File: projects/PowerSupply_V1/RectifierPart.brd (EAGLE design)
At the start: 50 x 50 mm, 17 parts, among them X1 IN, X2 PRI, X3 SEC, X4 OUT

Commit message: feat: rectifier power sources modified
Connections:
- new net +15VAC: F2.1, X3.1
- new net +20V: C1.1, C3.1, C5.+, D1.C, D3.C, X4.1
- new net -15VAC: C3.2, C4.1, D3.A, D4.C, X3.4
- new net -20V: C2.2, C4.2, C6.-, D2.A, D4.A, X4.3
- net V+: no longer C1.1, C3.1, C5.+, D1.C, D3.C, F2.1, X3.1, X4.1
- net V-: no longer C2.2, C3.2, C4.1, C4.2, C6.-, D2.A, D3.A, D4.A, D4.C, X3.4, X4.3
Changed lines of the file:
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@@
 <contactref element="F1" pad="2"/>
 <contactref element="R1" pad="2"/>
-<contactref element="X3" pad="1"/>
-<contactref element="F2" pad="1"/>
-<contactref element="D1" pad="C"/>
-<contactref element="D3" pad="C"/>
-<contactref element="C1" pad="1"/>
-<contactref element="C3" pad="1"/>
-<contactref element="C5" pad="+"/>
-<contactref element="X4" pad="1"/>
-<wire x1="45.847" y1="8.636" x2="45.847" y2="24.13" width="0" layer="19" extent="1-1"/>
-<wire x1="32.258" y1="4.572" x2="45.847" y2="8.636" width="0" layer="19" extent="1-1"/>
-<wire x1="4.191" y1="39.37" x2="45.847" y2="24.13" width="0" layer="19" extent="1-1"/>
 <wire x1="-14.1478" y1="31.75" x2="4.191" y2="39.37" width="0" layer="19" extent="1-1"/>
 <wire x1="-14.859" y1="16.51" x2="-14.1478" y2="31.75" width="0" layer="19" extent="1-1"/>
-<wire x1="-63.3222" y1="31.75" x2="-14.1478" y2="31.75" width="0" layer="19" extent="1-1"/>
-<wire x1="-63.5" y1="53.34" x2="-63.3222" y2="31.75" width="0" layer="19" extent="1-1"/>
-<wire x1="-50.8" y1="66.04" x2="-63.5" y2="53.34" width="0" layer="19" extent="1-1"/>
-<wire x1="-54.61" y1="74.93" x2="-50.8" y2="66.04" width="0" layer="19" extent="1-1"/>
-<wire x1="-39.37" y1="74.93" x2="-50.8" y2="66.04" width="0" layer="19" extent="1-1"/>
 </signal>
 <signal name="V-">
@@
 <contactref element="X2" pad="4"/>
 <contactref element="R1" pad="1"/>
-<contactref element="X3" pad="4"/>
-<contactref element="D3" pad="A"/>
-<contactref element="D4" pad="C"/>
-<contactref element="C3" pad="2"/>
-<contactref element="C4" pad="1"/>
-<contactref element="D2" pad="A"/>
-<contactref element="D4" pad="A"/>
-<contactref element="C2" pad="2"/>
-<contactref element="C4" pad="2"/>
-<contactref element="C6" pad="-"/>
-<contactref element="X4" pad="3"/>
-<wire x1="32.258" y1="28.956" x2="45.847" y2="39.37" width="0" layer="19" extent="1-1"/>
-<wire x1="45.847" y1="18.796" x2="32.258" y2="28.956" width="0" layer="19" extent="1-1"/>
-<wire x1="4.191" y1="34.29" x2="32.258" y2="28.956" width="0" layer="19" extent="1-1"/>
 <wire x1="4.191" y1="8.636" x2="4.191" y2="34.29" width="0" layer="19" extent="1-1"/>
 <wire x1="-18.161" y1="6.35" x2="4.191" y2="8.636" width="0" layer="19" extent="1-1"/>
-<wire x1="-15.24" y1="66.04" x2="4.191" y2="34.29" width="0" layer="19" extent="1-1"/>
-<wire x1="-15.24" y1="74.93" x2="-15.24" y2="66.04" width="0" layer="19" extent="1-1"/>
-<wire x1="-30.48" y1="74.93" x2="-15.24" y2="74.93" width="0" layer="19" extent="1-1"/>
-<wire x1="-35.56" y1="66.04" x2="-30.48" y2="74.93" width="0" layer="19" extent="1-1"/>
-<wire x1="-41.91" y1="74.93" x2="-35.56" y2="66.04" width="0" layer="19" extent="1-1"/>
-<wire x1="-49.53" y1="74.93" x2="-41.91" y2="74.93" width="0" layer="19" extent="1-1"/>
-<wire x1="-57.15" y1="74.93" x2="-49.53" y2="74.93" width="0" layer="19" extent="1-1"/>
-<wire x1="-62.23" y1="74.93" x2="-57.15" y2="74.93" width="0" layer="19" extent="1-1"/>
 </signal>
 <signal name="N$2">
@@
 <wire x1="-40.8178" y1="31.75" x2="-48.26" y2="53.34" width="0" layer="19" extent="1-1"/>
 </signal>
+<signal name="+20V">
+<contactref element="X4" pad="1"/>
+<contactref element="D1" pad="C"/>
+<contactref element="D3" pad="C"/>
+<contactref element="C1" pad="1"/>
+<contactref element="C3" pad="1"/>
+<contactref element="C5" pad="+"/>
+<wire x1="32.258" y1="4.572" x2="45.847" y2="8.636" width="0" layer="19" extent="1-1"/>
+<wire x1="-39.37" y1="74.93" x2="32.258" y2="4.572" width="0" layer="19" extent="1-1"/>
+<wire x1="-50.8" y1="66.04" x2="-39.37" y2="74.93" width="0" layer="19" extent="1-1"/>
+<wire x1="-54.61" y1="74.93" x2="-50.8" y2="66.04" width="0" layer="19" extent="1-1"/>
+<wire x1="-63.5" y1="53.34" x2="-50.8" y2="66.04" width="0" layer="19" extent="1-1"/>
+</signal>
+<signal name="-20V">
+<contactref element="X4" pad="3"/>
+<contactref element="D2" pad="A"/>
+<contactref element="D4" pad="A"/>
+<contactref element="C2" pad="2"/>
+<contactref element="C4" pad="2"/>
+<contactref element="C6" pad="-"/>
+<wire x1="32.258" y1="28.956" x2="45.847" y2="18.796" width="0" layer="19" extent="1-1"/>
+<wire x1="-15.24" y1="66.04" x2="32.258" y2="28.956" width="0" layer="19" extent="1-1"/>
+<wire x1="-15.24" y1="74.93" x2="-15.24" y2="66.04" width="0" layer="19" extent="1-1"/>
+<wire x1="-41.91" y1="74.93" x2="-15.24" y2="74.93" width="0" layer="19" extent="1-1"/>
+<wire x1="-57.15" y1="74.93" x2="-41.91" y2="74.93" width="0" layer="19" extent="1-1"/>
+</signal>
+<signal name="+15VAC">
+<contactref element="X3" pad="1"/>
+<contactref element="F2" pad="1"/>
+<wire x1="-63.3222" y1="31.75" x2="45.847" y2="24.13" width="0" layer="19" extent="1-1"/>
+</signal>
+<signal name="-15VAC">
+<contactref element="X3" pad="4"/>
+<contactref element="D3" pad="A"/>
+<contactref element="D4" pad="C"/>
+<contactref element="C3" pad="2"/>
+<contactref element="C4" pad="1"/>
+<wire x1="-30.48" y1="74.93" x2="45.847" y2="39.37" width="0" layer="19" extent="1-1"/>
+<wire x1="-35.56" y1="66.04" x2="-30.48" y2="74.93" width="0" layer="19" extent="1-1"/>
+<wire x1="-49.53" y1="74.93" x2="-35.56" y2="66.04" width="0" layer="19" extent="1-1"/>
+<wire x1="-62.23" y1="74.93" x2="-49.53" y2="74.93" width="0" layer="19" extent="1-1"/>
+</signal>
 </signals>

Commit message: feat: rectifier part modified
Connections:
- net V+ renamed +230VAC
- removed net V-: R1.1, X1.2, X2.4
- new net -230VAC: R1.1, X1.3, X2.4
- net PE: now also X1.2; no longer X1.3
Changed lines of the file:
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@@
 <signals>
 <signal name="GND">
-<contactref element="X3" pad="2"/>
-<contactref element="X3" pad="3"/>
 <contactref element="C6" pad="+"/>
 <contactref element="C5" pad="-"/>
 <contactref element="X4" pad="2"/>
+<contactref element="X3" pad="3"/>
+<contactref element="X3" pad="2"/>
 <wire x1="45.847" y1="29.21" x2="45.847" y2="34.29" width="0" layer="19" extent="1-1"/>
 <wire x1="45.847" y1="13.716" x2="45.847" y2="29.21" width="0" layer="19" extent="1-1"/>
 <wire x1="32.258" y1="12.192" x2="45.847" y2="13.716" width="0" layer="19" extent="1-1"/>
 <wire x1="32.258" y1="21.336" x2="32.258" y2="12.192" width="0" layer="19" extent="1-1"/>
-</signal>
-<signal name="PE">
-<contactref element="X1" pad="3"/>
-</signal>
-<signal name="V+">
-<contactref element="X1" pad="1"/>
-<contactref element="F1" pad="2"/>
-<contactref element="R1" pad="2"/>
-<wire x1="-14.1478" y1="31.75" x2="4.191" y2="39.37" width="0" layer="19" extent="1-1"/>
-<wire x1="-14.859" y1="16.51" x2="-14.1478" y2="31.75" width="0" layer="19" extent="1-1"/>
-</signal>
-<signal name="V-">
-<contactref element="X1" pad="2"/>
-<contactref element="X2" pad="4"/>
-<contactref element="R1" pad="1"/>
-<wire x1="4.191" y1="8.636" x2="4.191" y2="34.29" width="0" layer="19" extent="1-1"/>
-<wire x1="-18.161" y1="6.35" x2="4.191" y2="8.636" width="0" layer="19" extent="1-1"/>
 </signal>
 <signal name="N$2">
@@
 <wire x1="-40.8178" y1="31.75" x2="-48.26" y2="53.34" width="0" layer="19" extent="1-1"/>
 </signal>
-<signal name="+20V">
-<contactref element="X4" pad="1"/>
-<contactref element="D1" pad="C"/>
-<contactref element="D3" pad="C"/>
-<contactref element="C1" pad="1"/>
-<contactref element="C3" pad="1"/>
-<contactref element="C5" pad="+"/>
-<wire x1="32.258" y1="4.572" x2="45.847" y2="8.636" width="0" layer="19" extent="1-1"/>
-<wire x1="-39.37" y1="74.93" x2="32.258" y2="4.572" width="0" layer="19" extent="1-1"/>
-<wire x1="-50.8" y1="66.04" x2="-39.37" y2="74.93" width="0" layer="19" extent="1-1"/>
-<wire x1="-54.61" y1="74.93" x2="-50.8" y2="66.04" width="0" layer="19" extent="1-1"/>
-<wire x1="-63.5" y1="53.34" x2="-50.8" y2="66.04" width="0" layer="19" extent="1-1"/>
+<signal name="PE">
+<contactref element="X1" pad="2"/>
 </signal>
-<signal name="-20V">
-<contactref element="X4" pad="3"/>
-<contactref element="D2" pad="A"/>
-<contactref element="D4" pad="A"/>
-<contactref element="C2" pad="2"/>
-<contactref element="C4" pad="2"/>
-<contactref element="C6" pad="-"/>
-<wire x1="32.258" y1="28.956" x2="45.847" y2="18.796" width="0" layer="19" extent="1-1"/>
-<wire x1="-15.24" y1="66.04" x2="32.258" y2="28.956" width="0" layer="19" extent="1-1"/>
-<wire x1="-15.24" y1="74.93" x2="-15.24" y2="66.04" width="0" layer="19" extent="1-1"/>
-<wire x1="-41.91" y1="74.93" x2="-15.24" y2="74.93" width="0" layer="19" extent="1-1"/>
-<wire x1="-57.15" y1="74.93" x2="-41.91" y2="74.93" width="0" layer="19" extent="1-1"/>
+<signal name="+230VAC">
+<contactref element="X1" pad="1"/>
+<contactref element="F1" pad="2"/>
+<contactref element="R1" pad="2"/>
+<wire x1="-14.1478" y1="31.75" x2="4.191" y2="39.37" width="0" layer="19" extent="1-1"/>
+<wire x1="-14.859" y1="16.51" x2="-14.1478" y2="31.75" width="0" layer="19" extent="1-1"/>
+</signal>
+<signal name="-230VAC">
+<contactref element="X1" pad="3"/>
+<contactref element="X2" pad="4"/>
+<contactref element="R1" pad="1"/>
+<wire x1="4.191" y1="8.636" x2="4.191" y2="29.21" width="0" layer="19" extent="1-1"/>
+<wire x1="-18.161" y1="6.35" x2="4.191" y2="8.636" width="0" layer="19" extent="1-1"/>
 </signal>
 <signal name="+15VAC">
@@
 <wire x1="-62.23" y1="74.93" x2="-49.53" y2="74.93" width="0" layer="19" extent="1-1"/>
 </signal>
+<signal name="-20V">
+<contactref element="X4" pad="3"/>
+<contactref element="D2" pad="A"/>
+<contactref element="D4" pad="A"/>
+<contactref element="C2" pad="2"/>
+<contactref element="C4" pad="2"/>
+<contactref element="C6" pad="-"/>
+<wire x1="32.258" y1="28.956" x2="45.847" y2="18.796" width="0" layer="19" extent="1-1"/>
+<wire x1="-15.24" y1="66.04" x2="32.258" y2="28.956" width="0" layer="19" extent="1-1"/>
+<wire x1="-15.24" y1="74.93" x2="-15.24" y2="66.04" width="0" layer="19" extent="1-1"/>
+<wire x1="-41.91" y1="74.93" x2="-15.24" y2="74.93" width="0" layer="19" extent="1-1"/>
+<wire x1="-57.15" y1="74.93" x2="-41.91" y2="74.93" width="0" layer="19" extent="1-1"/>
+</signal>
+<signal name="+20V">
+<contactref element="X4" pad="1"/>
+<contactref element="D1" pad="C"/>
+<contactref element="D3" pad="C"/>
+<contactref element="C1" pad="1"/>
+<contactref element="C3" pad="1"/>
+<contactref element="C5" pad="+"/>
+<wire x1="32.258" y1="4.572" x2="45.847" y2="8.636" width="0" layer="19" extent="1-1"/>
+<wire x1="-39.37" y1="74.93" x2="32.258" y2="4.572" width="0" layer="19" extent="1-1"/>
+<wire x1="-50.8" y1="66.04" x2="-39.37" y2="74.93" width="0" layer="19" extent="1-1"/>
+<wire x1="-54.61" y1="74.93" x2="-50.8" y2="66.04" width="0" layer="19" extent="1-1"/>
+<wire x1="-63.5" y1="53.34" x2="-50.8" y2="66.04" width="0" layer="19" extent="1-1"/>
+</signal>
 </signals>

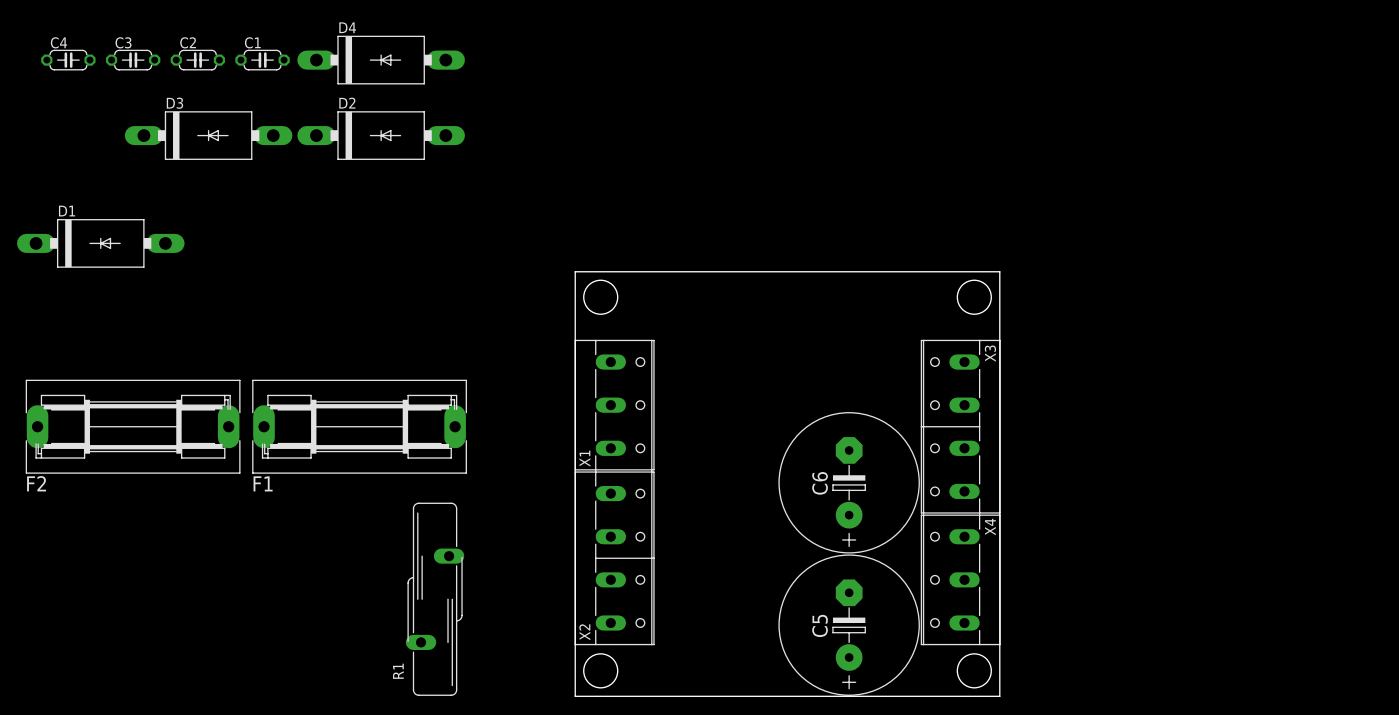
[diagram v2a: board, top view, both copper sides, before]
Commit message: feat: rectifier part refactored
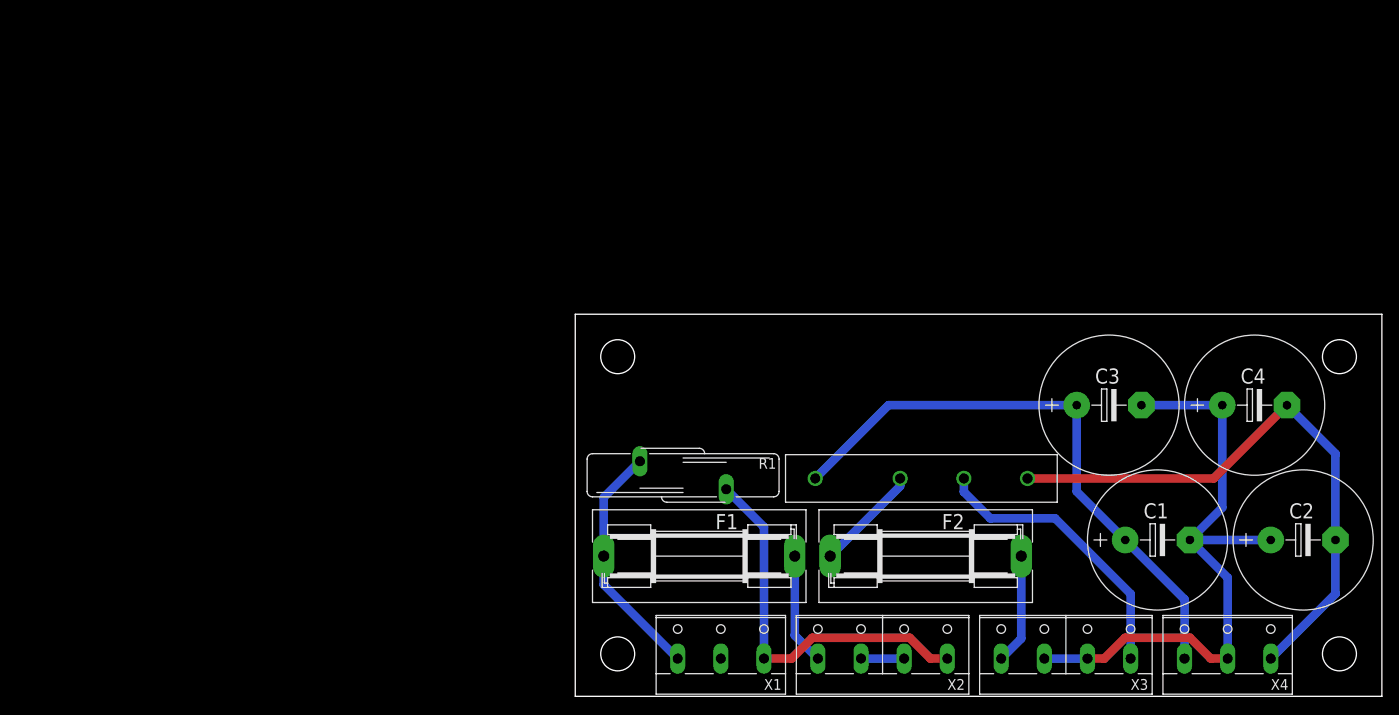
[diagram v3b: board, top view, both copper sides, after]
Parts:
- removed C5, C6: 2200µF, rcl:E7,5-16
- removed D1, D2, D3, D4: 10U45SD1, diode:DO201-15
- added R+1: B40C5000-3300A, bb84:B..C
- C1, C2, C3, C4: value 10nF -> 2200µF; device rcl:C050-024X044 -> rcl:E7,5-16
- moved C4 145.5 mm to (80.0, 34.3)
- moved C2 141.9 mm to (85.7, 18.4)
- moved C3 121.9 mm to (62.9, 34.3)
- moved C1 119.6 mm to (68.6, 18.4)
- moved F2 94.6 mm to (41.3, 16.5), turned to 180 degrees
- moved F1 42.8 mm to (14.6, 16.5), turned to 180 degrees
- moved X2 33.3 mm to (36.2, 5.08), turned to 0 degrees
- moved X4 32.8 mm to (76.8, 5.08), turned to 0 degrees
- moved R1 32.7 mm to (12.7, 26.0), turned to 90 degrees
- moved X1 31.7 mm to (17.1, 5.08), turned to 0 degrees
- moved X3 29.5 mm to (57.8, 5.08), turned to 0 degrees
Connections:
- removed net N$5: C1.2, C2.1, D1.A, D2.C, F2.2
- new net N$1: F2.2, R+1.~VAC1
- net +20V: now also C1.+, C3.+, R+1.+VDC; no longer C1.1, C3.1, C5.+, D1.C, D3.C
- net -15VAC: now also R+1.~VAC2; no longer C3.2, C4.1, D3.A, D4.C
- net -20V: now also C2.-, C4.-, R+1.-VDC; no longer C2.2, C4.2, C6.-, D2.A, D4.A
- net GND: now also C1.-, C2.+, C3.-, C4.+; no longer C5.-, C6.+
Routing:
- net GND: track 0.00 -> 75.9 mm
- net -20V: track 0.00 -> 69.5 mm
- net +20V: track 0.00 -> 69.5 mm
- net -230VAC: track 0.00 -> 45.4 mm
- net -15VAC: track 0.00 -> 33.8 mm
- net +230VAC: track 0.00 -> 28.6 mm
- net N$3: track 0.00 -> 13.2 mm
- net +15VAC: track 0.00 -> 13.0 mm
- net N$1: track 0.00 -> 12.6 mm
- net N$2: track 0.00 -> 5.08 mm
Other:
- board size 50 x 50 mm -> 95 x 45 mm

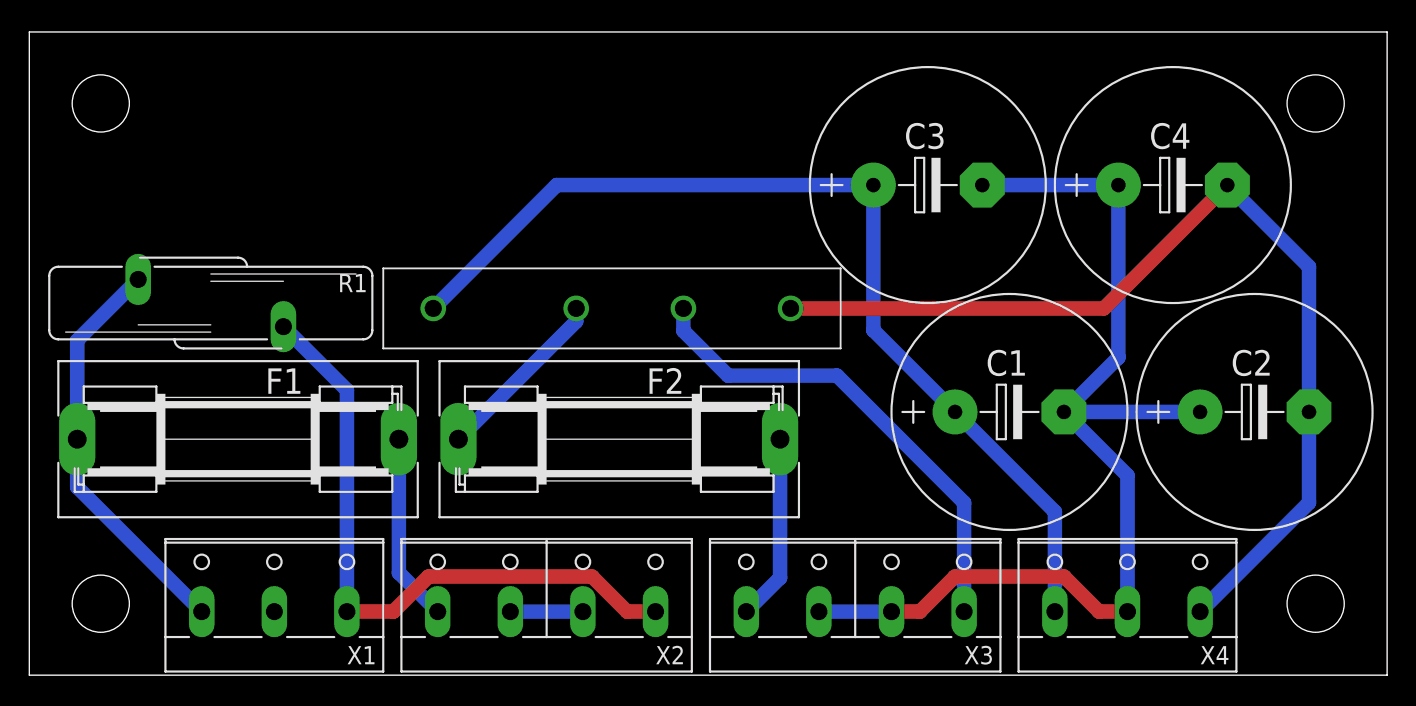
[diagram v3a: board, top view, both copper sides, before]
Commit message: feat: rectifier part modified
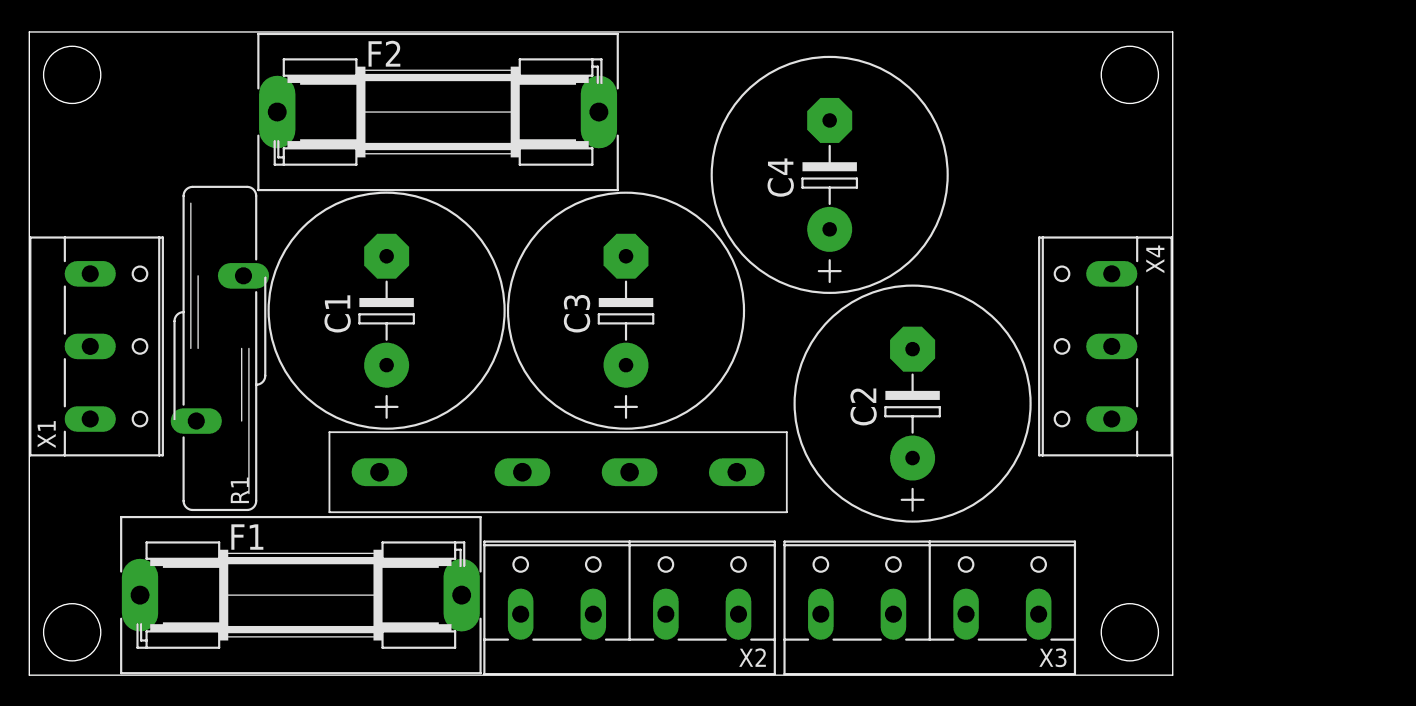
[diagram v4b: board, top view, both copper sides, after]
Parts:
- moved C1 44.2 mm to (25.0, 25.5), turned to 90 degrees
- moved F2 26.2 mm to (28.6, 39.4)
- moved C4 24.0 mm to (56.0, 35.0), turned to 90 degrees
- moved C2 23.9 mm to (61.8, 19.0), turned to 90 degrees
- moved C3 22.9 mm to (41.8, 25.5), turned to 90 degrees
- moved X1 21.7 mm to (4.90, 23.0), turned to 270 degrees
- moved X4 18.0 mm to (75.1, 23.0), turned to 90 degrees
- moved R+1 12.1 mm to (21.0, 11.4)
- moved F1 11.8 mm to (19.0, 5.60)
- moved X2 5.81 mm to (42.0, 4.90)
- moved X3 5.22 mm to (63.0, 4.90)
- moved R1 3.24 mm to (13.3, 22.9), turned to 0 degrees
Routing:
- net GND: track 75.9 -> 0.00 mm
- net -20V: track 69.5 -> 0.00 mm
- net +20V: track 69.5 -> 0.00 mm
- net -230VAC: track 45.4 -> 0.00 mm
- net -15VAC: track 33.8 -> 0.00 mm
- net +230VAC: track 28.6 -> 0.00 mm
- net N$3: track 13.2 -> 0.00 mm
- net +15VAC: track 13.0 -> 0.00 mm
- net N$1: track 12.6 -> 0.00 mm
- net N$2: track 5.08 -> 0.00 mm
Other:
- board size 95 x 45 mm -> 80 x 45 mm
